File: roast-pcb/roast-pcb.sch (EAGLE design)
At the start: 3 parts

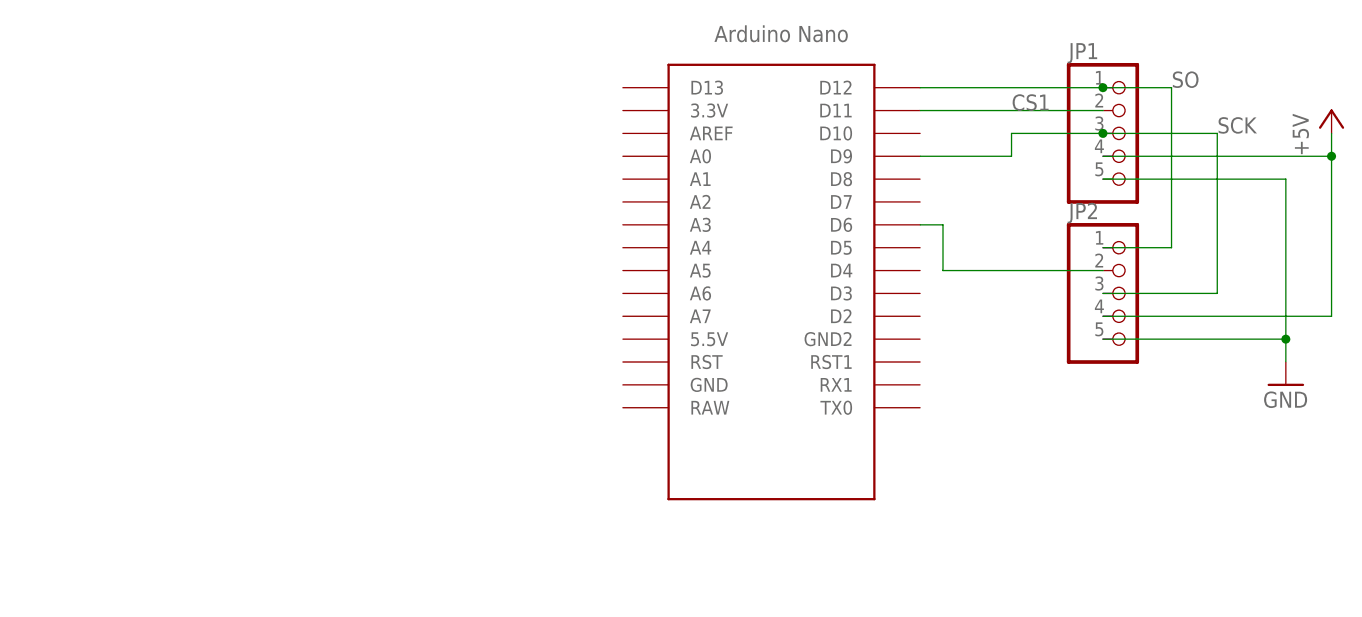
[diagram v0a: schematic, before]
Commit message: ready to print PCB design
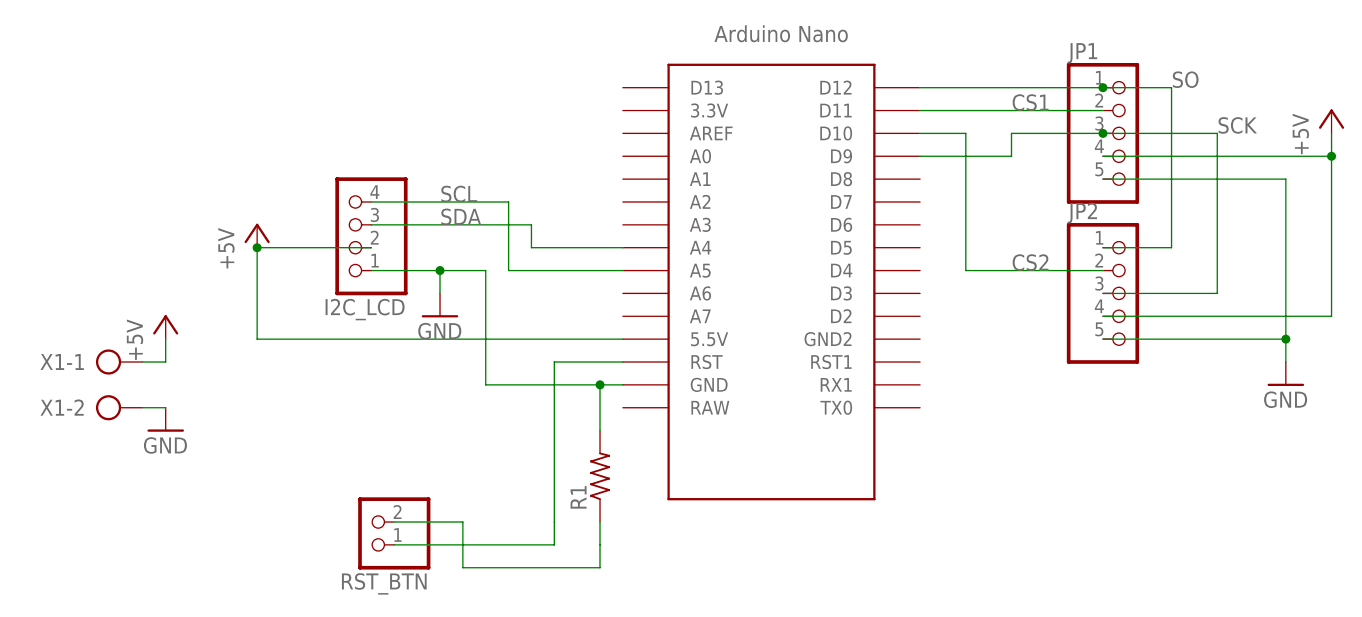
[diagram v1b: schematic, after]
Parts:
- added I2C_LCD: (no value), pinhead:PINHD-1X4
- added R1: (no value), rcl:R-US_0207/10
- added RST_BTN: (no value), pinhead:PINHD-1X2
- added X1: (no value), con-ptr500:AK300/2
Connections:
- new net CS2: JP2.2, U$1.D10
- new net N$5: R1.1, RST_BTN.2
- new net SCL: I2C_LCD.4, U$1.A5
- new net SDA: I2C_LCD.3, U$1.A4
- net +5V: now also I2C_LCD.2, U$1.5.5V, X1-1.KL
- net GND: now also I2C_LCD.1, R1.2, U$1.GND, X1-2.KL
- net N$1: now also RST_BTN.1, U$1.RST; no longer JP2.2, U$1.D6
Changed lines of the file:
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@@
 <part name="P+1" library="supply1" library_urn="urn:adsk.eagle:library:371" deviceset="+5V" device=""/>
 <part name="GND1" library="supply1" library_urn="urn:adsk.eagle:library:371" deviceset="GND" device=""/>
+<part name="I2C_LCD" library="pinhead" library_urn="urn:adsk.eagle:library:325" deviceset="PINHD-1X4" device="" package3d_urn="urn:adsk.eagle:package:22407/2"/>
+<part name="GND2" library="supply1" library_urn="urn:adsk.eagle:library:371" deviceset="GND" device=""/>
+<part name="P+2" library="supply1" library_urn="urn:adsk.eagle:library:371" deviceset="+5V" device=""/>
+<part name="RST_BTN" library="pinhead" library_urn="urn:adsk.eagle:library:325" deviceset="PINHD-1X2" device="" package3d_urn="urn:adsk.eagle:package:22435/2"/>
+<part name="R1" library="rcl" library_urn="urn:adsk.eagle:library:334" deviceset="R-US_" device="0207/10" package3d_urn="urn:adsk.eagle:package:23491/1"/>
+<part name="X1" library="con-ptr500" library_urn="urn:adsk.eagle:library:181" deviceset="AK300/2" device="" package3d_urn="urn:adsk.eagle:package:9881/1"/>
+<part name="P+3" library="supply1" library_urn="urn:adsk.eagle:library:371" deviceset="+5V" device=""/>
+<part name="GND3" library="supply1" library_urn="urn:adsk.eagle:library:371" deviceset="GND" device=""/>
 </parts>
 <sheets>
@@
 <instance part="P+1" gate="1" x="121.92" y="73.66"/>
 <instance part="GND1" gate="1" x="116.84" y="43.18"/>
+<instance part="I2C_LCD" gate="A" x="12.7" y="60.96" rot="R180"/>
+<instance part="GND2" gate="1" x="22.86" y="50.8"/>
+<instance part="P+2" gate="1" x="2.54" y="60.96"/>
+<instance part="RST_BTN" gate="G$1" x="15.24" y="27.94" rot="R180"/>
+<instance part="R1" gate="G$1" x="40.64" y="33.02" rot="R90"/>
+<instance part="X1" gate="-1" x="-15.24" y="45.72"/>
+<instance part="X1" gate="-2" x="-15.24" y="40.64"/>
+<instance part="P+3" gate="1" x="-7.62" y="50.8"/>
+<instance part="GND3" gate="1" x="-7.62" y="38.1"/>
 </instances>
 <busses>
@@
 <junction x="121.92" y="68.58"/>
 </segment>
+<segment>
+<pinref part="P+2" gate="1" pin="+5V"/>
+<pinref part="I2C_LCD" gate="A" pin="2"/>
+<wire x1="2.54" y1="58.42" x2="15.24" y2="58.42" width="0.1524" layer="91"/>
+<pinref part="U$1" gate="G$1" pin="5.5V"/>
+<wire x1="43.18" y1="48.26" x2="2.54" y2="48.26" width="0.1524" layer="91"/>
+<wire x1="2.54" y1="48.26" x2="2.54" y2="58.42" width="0.1524" layer="91"/>
+<junction x="2.54" y="58.42"/>
+</segment>
+<segment>
+<pinref part="X1" gate="-1" pin="KL"/>
+<wire x1="-10.16" y1="45.72" x2="-7.62" y2="45.72" width="0.1524" layer="91"/>
+<pinref part="P+3" gate="1" pin="+5V"/>
+<wire x1="-7.62" y1="45.72" x2="-7.62" y2="48.26" width="0.1524" layer="91"/>
+</segment>
 </net>
 <net name="GND" class="0">
@@
 <junction x="116.84" y="48.26"/>
 </segment>
+<segment>
+<pinref part="I2C_LCD" gate="A" pin="1"/>
+<wire x1="15.24" y1="55.88" x2="22.86" y2="55.88" width="0.1524" layer="91"/>
+<pinref part="GND2" gate="1" pin="GND"/>
+<wire x1="22.86" y1="55.88" x2="22.86" y2="53.34" width="0.1524" layer="91"/>
+<junction x="22.86" y="55.88"/>
+<wire x1="22.86" y1="55.88" x2="27.94" y2="55.88" width="0.1524" layer="91"/>
+<wire x1="27.94" y1="55.88" x2="27.94" y2="43.18" width="0.1524" layer="91"/>
+<pinref part="U$1" gate="G$1" pin="GND"/>
+<wire x1="27.94" y1="43.18" x2="40.64" y2="43.18" width="0.1524" layer="91"/>
+<pinref part="R1" gate="G$1" pin="2"/>
+<wire x1="40.64" y1="43.18" x2="43.18" y2="43.18" width="0.1524" layer="91"/>
+<wire x1="40.64" y1="38.1" x2="40.64" y2="43.18" width="0.1524" layer="91"/>
+<junction x="40.64" y="43.18"/>
+</segment>
+<segment>
+<pinref part="X1" gate="-2" pin="KL"/>
+<pinref part="GND3" gate="1" pin="GND"/>
+<wire x1="-10.16" y1="40.64" x2="-7.62" y2="40.64" width="0.1524" layer="91"/>
+</segment>
+</net>
+<net name="CS2" class="0">
+<segment>
+<pinref part="U$1" gate="G$1" pin="D10"/>
+<wire x1="76.2" y1="71.12" x2="81.28" y2="71.12" width="0.1524" layer="91"/>
+<wire x1="81.28" y1="71.12" x2="81.28" y2="55.88" width="0.1524" layer="91"/>
+<pinref part="JP2" gate="A" pin="2"/>
+<wire x1="81.28" y1="55.88" x2="96.52" y2="55.88" width="0.1524" layer="91"/>
+<label x="86.36" y="55.88" size="1.778" layer="95"/>
+</segment>
+</net>
+<net name="SDA" class="0">
+<segment>
+<pinref part="I2C_LCD" gate="A" pin="3"/>
+<wire x1="15.24" y1="60.96" x2="33.02" y2="60.96" width="0.1524" layer="91"/>
+<wire x1="33.02" y1="60.96" x2="33.02" y2="58.42" width="0.1524" layer="91"/>
+<pinref part="U$1" gate="G$1" pin="A4"/>
+<wire x1="33.02" y1="58.42" x2="43.18" y2="58.42" width="0.1524" layer="91"/>
+<label x="22.86" y="60.96" size="1.778" layer="95"/>
+</segment>
 </net>
 <net name="N$1" class="0">
 <segment>
-<pinref part="JP2" gate="A" pin="2"/>
-<wire x1="96.52" y1="55.88" x2="78.74" y2="55.88" width="0.1524" layer="91"/>
-<wire x1="78.74" y1="55.88" x2="78.74" y2="60.96" width="0.1524" layer="91"/>
-<pinref part="U$1" gate="G$1" pin="D6"/>
-<wire x1="78.74" y1="60.96" x2="76.2" y2="60.96" width="0.1524" layer="91"/>
+<pinref part="U$1" gate="G$1" pin="RST"/>
+<wire x1="35.56" y1="27.94" x2="35.56" y2="45.72" width="0.1524" layer="91"/>
+<wire x1="35.56" y1="45.72" x2="43.18" y2="45.72" width="0.1524" layer="91"/>
+<pinref part="RST_BTN" gate="G$1" pin="1"/>
+<wire x1="17.78" y1="25.4" x2="35.56" y2="25.4" width="0.1524" layer="91"/>
+<wire x1="35.56" y1="25.4" x2="35.56" y2="27.94" width="0.1524" layer="91"/>
+</segment>
+</net>
+<net name="N$5" class="0">
+<segment>
+<pinref part="R1" gate="G$1" pin="1"/>
+<wire x1="40.64" y1="27.94" x2="40.64" y2="25.4" width="0.1524" layer="91"/>
+<wire x1="40.64" y1="25.4" x2="40.64" y2="22.86" width="0.1524" layer="91"/>
+<wire x1="40.64" y1="22.86" x2="25.4" y2="22.86" width="0.1524" layer="91"/>
+<wire x1="25.4" y1="22.86" x2="25.4" y2="27.94" width="0.1524" layer="91"/>
+<pinref part="RST_BTN" gate="G$1" pin="2"/>
+<wire x1="25.4" y1="27.94" x2="17.78" y2="27.94" width="0.1524" layer="91"/>
+</segment>
+</net>
+<net name="SCL" class="0">
+<segment>
+<pinref part="I2C_LCD" gate="A" pin="4"/>
+<wire x1="15.24" y1="63.5" x2="30.48" y2="63.5" width="0.1524" layer="91"/>
+<pinref part="U$1" gate="G$1" pin="A5"/>
+<wire x1="30.48" y1="63.5" x2="30.48" y2="55.88" width="0.1524" layer="91"/>
+<wire x1="30.48" y1="55.88" x2="43.18" y2="55.88" width="0.1524" layer="91"/>
+<label x="22.86" y="63.5" size="1.778" layer="95"/>
 </segment>
 </net>
@@
 packages will not be understood (or retained) with this version.
 </note>
+<note version="8.4" severity="warning">
+Since Version 8.4, EAGLE supports properties for SPICE simulation.
+Probes in schematics and SPICE mapping objects found in parts and library devices
+will not be understood with this version. Update EAGLE to the latest version
+for full support of SPICE simulation.
+</note>
 </compatibility>

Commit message: test ready sensor
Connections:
- new net N$4: U$1.RAW, X1-1.KL
- net +5V: no longer X1-1.KL
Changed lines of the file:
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@@
 <part name="R1" library="rcl" library_urn="urn:adsk.eagle:library:334" deviceset="R-US_" device="0207/10" package3d_urn="urn:adsk.eagle:package:23491/1"/>
 <part name="X1" library="con-ptr500" library_urn="urn:adsk.eagle:library:181" deviceset="AK300/2" device="" package3d_urn="urn:adsk.eagle:package:9881/1"/>
-<part name="P+3" library="supply1" library_urn="urn:adsk.eagle:library:371" deviceset="+5V" device=""/>
 <part name="GND3" library="supply1" library_urn="urn:adsk.eagle:library:371" deviceset="GND" device=""/>
 </parts>
@@
 <instance part="X1" gate="-1" x="-15.24" y="45.72"/>
 <instance part="X1" gate="-2" x="-15.24" y="40.64"/>
-<instance part="P+3" gate="1" x="-7.62" y="50.8"/>
 <instance part="GND3" gate="1" x="-7.62" y="38.1"/>
 </instances>
@@
 <wire x1="2.54" y1="48.26" x2="2.54" y2="58.42" width="0.1524" layer="91"/>
 <junction x="2.54" y="58.42"/>
-</segment>
-<segment>
-<pinref part="X1" gate="-1" pin="KL"/>
-<wire x1="-10.16" y1="45.72" x2="-7.62" y2="45.72" width="0.1524" layer="91"/>
-<pinref part="P+3" gate="1" pin="+5V"/>
-<wire x1="-7.62" y1="45.72" x2="-7.62" y2="48.26" width="0.1524" layer="91"/>
 </segment>
 </net>
@@
 </segment>
 </net>
+<net name="N$4" class="0">
+<segment>
+<pinref part="X1" gate="-1" pin="KL"/>
+<wire x1="-10.16" y1="45.72" x2="-2.54" y2="45.72" width="0.1524" layer="91"/>
+<pinref part="U$1" gate="G$1" pin="RAW"/>
+<wire x1="-2.54" y1="45.72" x2="-2.54" y2="40.64" width="0.1524" layer="91"/>
+<wire x1="-2.54" y1="40.64" x2="43.18" y2="40.64" width="0.1524" layer="91"/>
+</segment>
+</net>
